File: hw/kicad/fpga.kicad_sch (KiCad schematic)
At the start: 18 parts, among them U201 W25Q64JVSSIQ

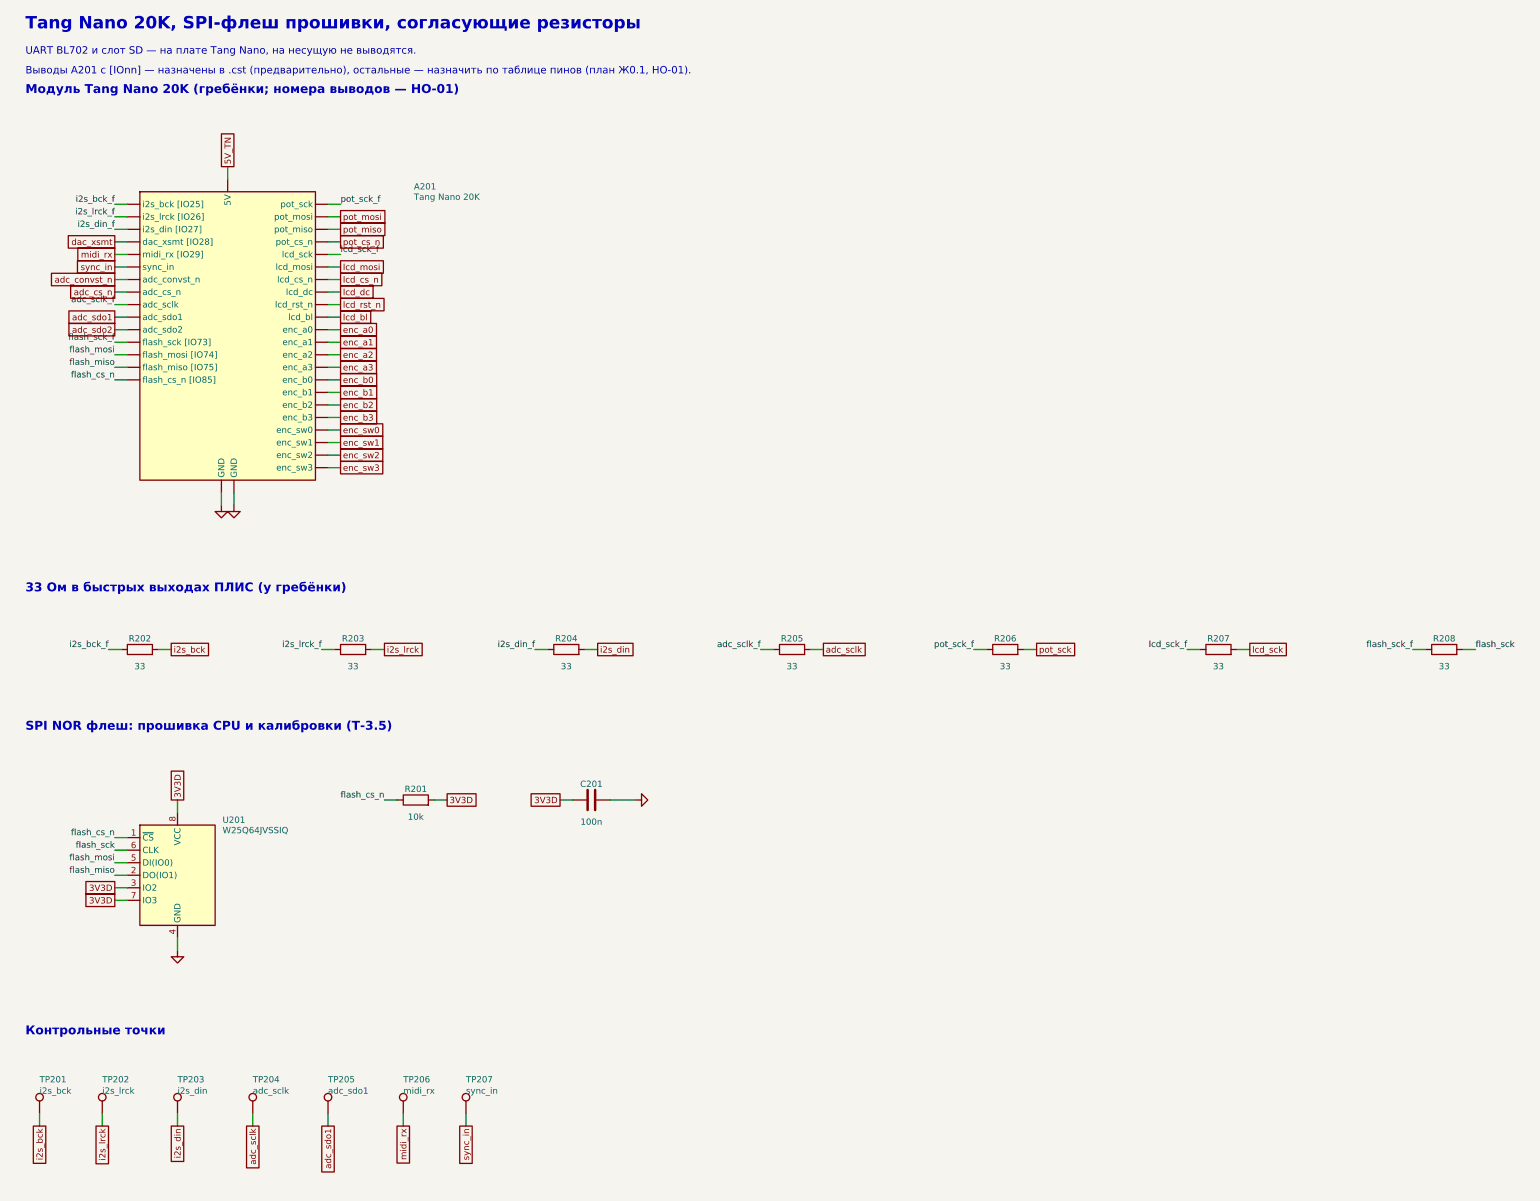
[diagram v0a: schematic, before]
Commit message: Reorganize KiCad schematic into 7 functional sheets with framed blocks
- Sheets: power, fpga, midi_sync, analog_in (inputs + ADC), audio_out
  (DAC + OUT/OUT2 + clip LEDs), phones, panel
- Each functional block is drawn in a dashed frame with a title; blocks are
  tiled across the sheet, A3/A2 chosen automatically
- Netlist check still 153/153; PDF and docs updated

Co-Authored-By: Claude Opus 5.5 <noreply@anthropic.com>
Claude-Session: https://claude.ai/code/session_01JcNV2ZCXWxtNzRVWffkrjk
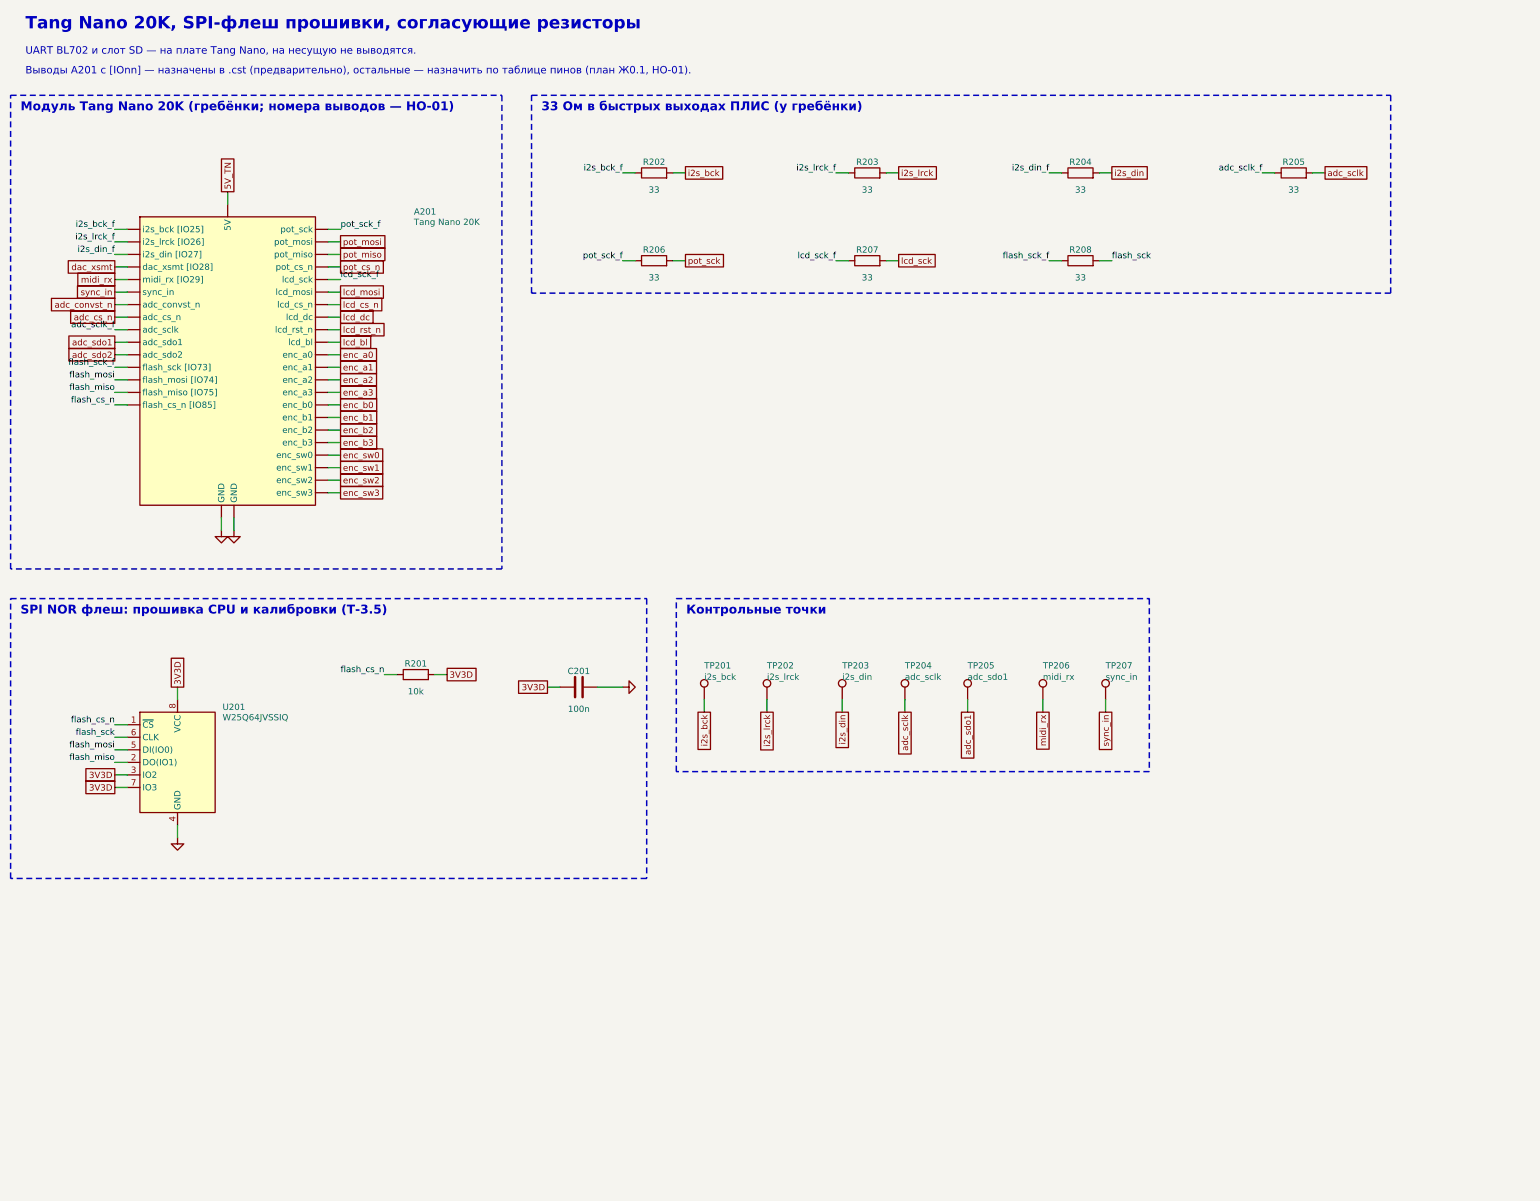
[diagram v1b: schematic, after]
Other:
- moved on the sheet: A201, C201, R201, R202, R203, R204, R205, R206, R207, R208, TP201, TP202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
